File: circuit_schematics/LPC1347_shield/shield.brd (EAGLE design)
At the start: 94.9 x 35.5 mm, 17 parts, among them IC1 7805TV, IC2 LD1117V33

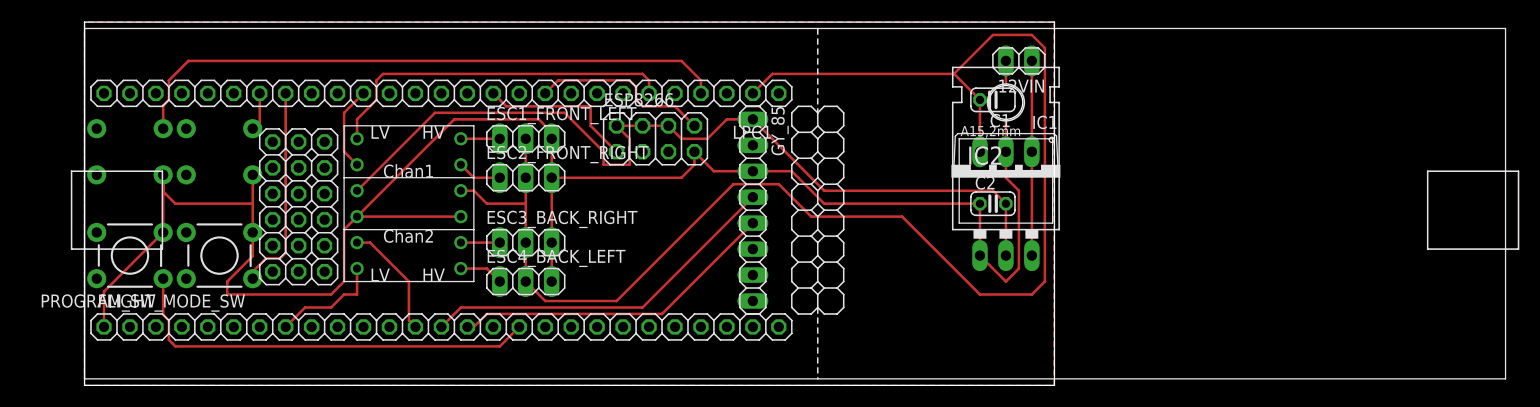
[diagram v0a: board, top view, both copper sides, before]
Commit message: Moved all traces to back and fixed all errors.
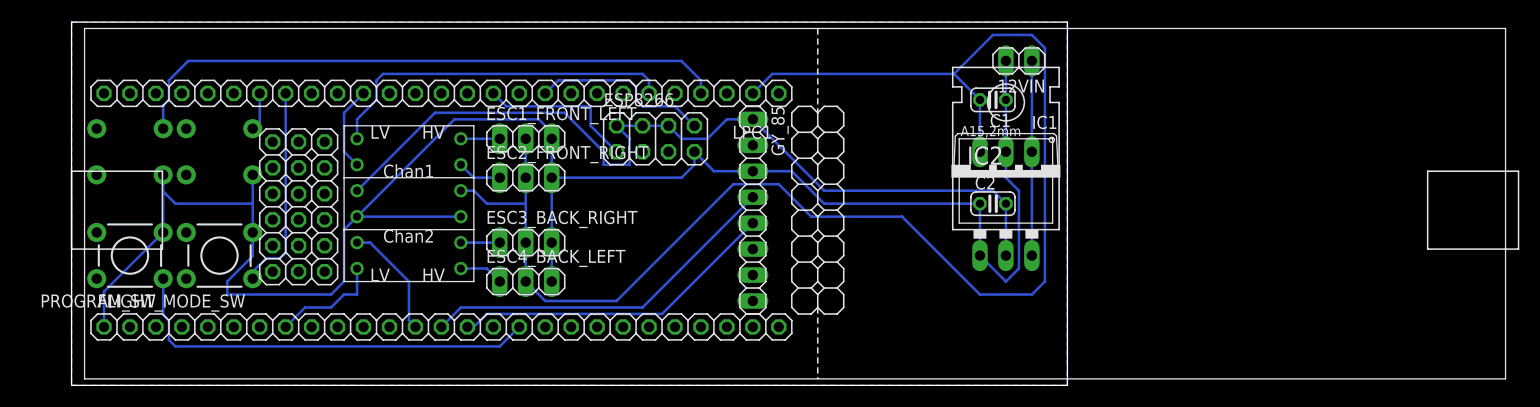
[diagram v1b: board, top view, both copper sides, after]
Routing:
- net GND: track 185.1 -> 183.5 mm
- added copper zone on layer 16, net N$1
- removed copper zone on layer 1, net N$1
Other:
- board size 94.9 x 35.5 mm -> 97.5 x 35.5 mm

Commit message: Hid unnecessary layers.
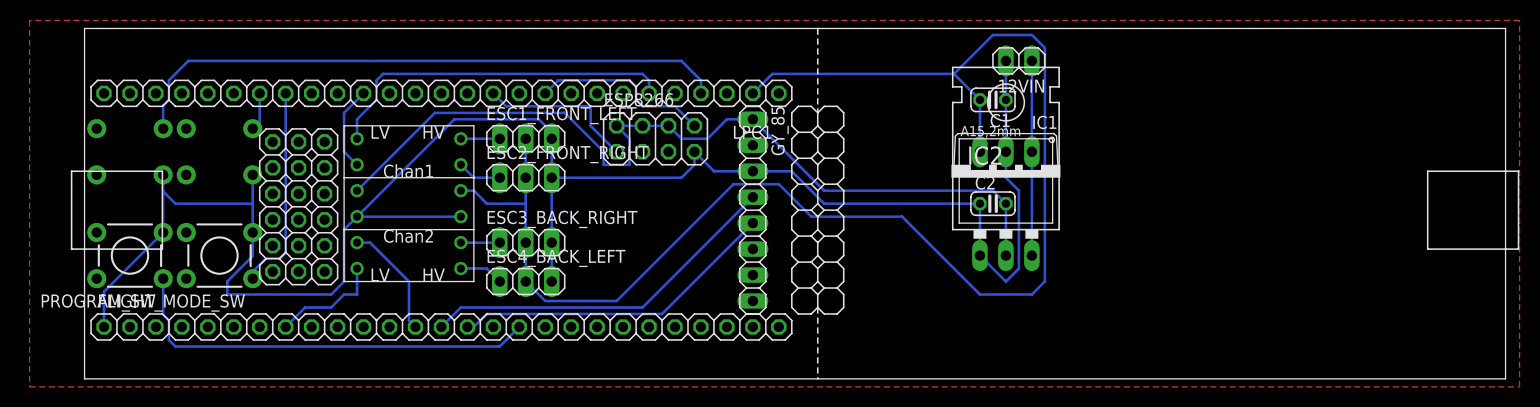
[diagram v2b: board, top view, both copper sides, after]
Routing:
- added copper zone on layer 1, net _OUTLINES_
- removed copper zone on layer 16, net N$1
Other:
- board outline removed
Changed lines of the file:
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@@
 <grid distance="0.05" unitdist="inch" unit="inch" style="lines" multiple="1" display="yes" altdistance="0.005" altunitdist="inch" altunit="inch"/>
 <layers>
-<layer number="1" name="Top" color="4" fill="1" visible="yes" active="yes"/>
+<layer number="1" name="Top" color="4" fill="1" visible="no" active="yes"/>
 <layer number="16" name="Bottom" color="1" fill="1" visible="yes" active="yes"/>
 <layer number="17" name="Pads" color="2" fill="1" visible="yes" active="yes"/>
@@
 <layer number="20" name="Dimension" color="15" fill="1" visible="yes" active="yes"/>
 <layer number="21" name="tPlace" color="7" fill="1" visible="yes" active="yes"/>
-<layer number="22" name="bPlace" color="7" fill="1" visible="yes" active="yes"/>
-<layer number="23" name="tOrigins" color="15" fill="1" visible="yes" active="yes"/>
-<layer number="24" name="bOrigins" color="15" fill="1" visible="yes" active="yes"/>
-<layer number="25" name="tNames" color="7" fill="1" visible="yes" active="yes"/>
-<layer number="26" name="bNames" color="7" fill="1" visible="yes" active="yes"/>
-<layer number="27" name="tValues" color="7" fill="1" visible="yes" active="yes"/>
-<layer number="28" name="bValues" color="7" fill="1" visible="yes" active="yes"/>
+<layer number="22" name="bPlace" color="7" fill="1" visible="no" active="yes"/>
+<layer number="23" name="tOrigins" color="15" fill="1" visible="no" active="yes"/>
+<layer number="24" name="bOrigins" color="15" fill="1" visible="no" active="yes"/>
+<layer number="25" name="tNames" color="7" fill="1" visible="no" active="yes"/>
+<layer number="26" name="bNames" color="7" fill="1" visible="no" active="yes"/>
+<layer number="27" name="tValues" color="7" fill="1" visible="no" active="yes"/>
+<layer number="28" name="bValues" color="7" fill="1" visible="no" active="yes"/>
 <layer number="29" name="tStop" color="7" fill="3" visible="no" active="yes"/>
 <layer number="30" name="bStop" color="7" fill="6" visible="no" active="yes"/>
@@
 <layer number="46" name="Milling" color="3" fill="1" visible="no" active="yes"/>
 <layer number="47" name="Measures" color="7" fill="1" visible="no" active="yes"/>
-<layer number="48" name="Document" color="7" fill="1" visible="yes" active="yes"/>
+<layer number="48" name="Document" color="7" fill="1" visible="no" active="yes"/>
 <layer number="49" name="Reference" color="7" fill="1" visible="yes" active="yes"/>
 <layer number="50" name="dxf" color="7" fill="1" visible="no" active="no"/>
-<layer number="51" name="tDocu" color="7" fill="1" visible="yes" active="yes"/>
-<layer number="52" name="bDocu" color="7" fill="1" visible="yes" active="yes"/>
+<layer number="51" name="tDocu" color="7" fill="1" visible="no" active="yes"/>
+<layer number="52" name="bDocu" color="7" fill="1" visible="no" active="yes"/>
 <layer number="53" name="tGND_GNDA" color="7" fill="9" visible="no" active="no"/>
 <layer number="54" name="bGND_GNDA" color="1" fill="9" visible="no" active="no"/>
@@
 <layer number="101" name="Patch_Top" color="12" fill="4" visible="yes" active="yes"/>
 <layer number="102" name="Vscore" color="7" fill="1" visible="yes" active="yes"/>
-<layer number="103" name="tMap" color="7" fill="1" visible="yes" active="yes"/>
-<layer number="104" name="Name" color="16" fill="1" visible="yes" active="yes"/>
+<layer number="103" name="tMap" color="7" fill="1" visible="no" active="yes"/>
+<layer number="104" name="Name" color="16" fill="1" visible="no" active="yes"/>
 <layer number="105" name="tPlate" color="7" fill="1" visible="yes" active="yes"/>
 <layer number="106" name="bPlate" color="7" fill="1" visible="yes" active="yes"/>
@@
 <layer number="110" name="fp0" color="7" fill="1" visible="yes" active="yes"/>
 <layer number="111" name="LPC17xx" color="7" fill="1" visible="yes" active="yes"/>
-<layer number="112" name="tSilk" color="7" fill="1" visible="yes" active="yes"/>
+<layer number="112" name="tSilk" color="7" fill="1" visible="no" active="yes"/>
 <layer number="113" name="IDFDebug" color="7" fill="1" visible="yes" active="yes"/>
 <layer number="114" name="Badge_Outline" color="11" fill="1" visible="no" active="no"/>
 <layer number="116" name="Patch_BOT" color="9" fill="4" visible="yes" active="yes"/>
 <layer number="118" name="Rect_Pads" color="7" fill="1" visible="yes" active="yes"/>
-<layer number="121" name="_tsilk" color="7" fill="1" visible="yes" active="yes"/>
-<layer number="122" name="_bsilk" color="7" fill="1" visible="yes" active="yes"/>
+<layer number="121" name="_tsilk" color="7" fill="1" visible="no" active="yes"/>
+<layer number="122" name="_bsilk" color="7" fill="1" visible="no" active="yes"/>
 <layer number="123" name="tTestmark" color="7" fill="1" visible="yes" active="yes"/>
 <layer number="124" name="bTestmark" color="7" fill="1" visible="yes" active="yes"/>
-<layer number="125" name="_tNames" color="7" fill="1" visible="yes" active="yes"/>
-<layer number="126" name="_bNames" color="7" fill="1" visible="yes" active="yes"/>
-<layer number="127" name="_tValues" color="7" fill="1" visible="yes" active="yes"/>
-<layer number="128" name="_bValues" color="7" fill="1" visible="yes" active="yes"/>
-<layer number="129" name="Mask" color="7" fill="1" visible="yes" active="yes"/>
+<layer number="125" name="_tNames" color="7" fill="1" visible="no" active="yes"/>
+<layer number="126" name="_bNames" color="7" fill="1" visible="no" active="yes"/>
+<layer number="127" name="_tValues" color="7" fill="1" visible="no" active="yes"/>
+<layer number="128" name="_bValues" color="7" fill="1" visible="no" active="yes"/>
+<layer number="129" name="Mask" color="7" fill="1" visible="no" active="yes"/>
 <layer number="131" name="tAdjust" color="7" fill="1" visible="yes" active="yes"/>
 <layer number="132" name="bAdjust" color="7" fill="1" visible="yes" active="yes"/>
@@
 <layer number="150" name="Notes" color="7" fill="1" visible="yes" active="yes"/>
 <layer number="151" name="HeatSink" color="7" fill="1" visible="yes" active="yes"/>
-<layer number="152" name="_bDocu" color="7" fill="1" visible="yes" active="yes"/>
+<layer number="152" name="_bDocu" color="7" fill="1" visible="no" active="yes"/>
 <layer number="153" name="FabDoc1" color="7" fill="1" visible="yes" active="yes"/>
 <layer number="154" name="FabDoc2" color="7" fill="1" visible="yes" active="yes"/>
@@
 <board>
 <plain>
-<wire x1="-1.27" y1="0" x2="96.19" y2="0" width="0" layer="20"/>
-<wire x1="96.19" y1="0" x2="96.19" y2="35.55" width="0" layer="20"/>
-<wire x1="96.19" y1="35.55" x2="-1.27" y2="35.55" width="0" layer="20"/>
-<wire x1="-1.27" y1="35.55" x2="-1.27" y2="0" width="0" layer="20"/>
 </plain>
 <attributes>
@@
 <wire x1="31.75" y1="6.35" x2="32.385" y2="5.715" width="0.254" layer="16"/>
 </signal>
-<signal name="N$1">
-<polygon width="0.254" layer="16" isolate="0.3048">
-<vertex x="96.139" y="0"/>
-<vertex x="96.139" y="35.56"/>
-<vertex x="-1.27" y="35.56"/>
-<vertex x="-1.27" y="0"/>
+<signal name="_OUTLINES_">
+<polygon width="0.3048" layer="1" isolate="0.5334" orphans="yes" rank="6">
+<vertex x="-5.37085625" y="-0.1524"/>
+<vertex x="140.4366" y="-0.1524"/>
+<vertex x="140.4366" y="35.7124"/>
+<vertex x="-5.37085625" y="35.7124"/>
 </polygon>
 </signal>
